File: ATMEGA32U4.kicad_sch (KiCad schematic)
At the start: 4 parts, among them U2 ATMEGA32U4-AU, U3 MIC5219-3_3YM5-TR

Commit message: improvements
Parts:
- added C14, C15, C18: 0.1uF, Capacitor_SMD:C_0805_2012Metric, symbol Device:C_Small
- added C16, C17: 22pF, Capacitor_SMD:C_0805_2012Metric, symbol Device:C_Small
- added C19: 10uF, Capacitor_SMD:C_0805_2012Metric, symbol Device:C_Small
- added C20: 1uF, Capacitor_SMD:C_0805_2012Metric, symbol Device:C_Small
- added J5: Conn_01x04, random-keyboard-parts:JST-SR-4, symbol Connector_Generic:Conn_01x04
- added RC1, RC2: 22, Resistor_SMD:R_0805_2012Metric, symbol Device:R_Small
- added RC3, RC4: 10k, Resistor_SMD:R_0805_2012Metric, symbol Device:R_Small
- added SW1: SW_Push, Button_Switch_SMD:SW_SPST_PTS645, symbol Switch:SW_Push
- added Y1: 16MHz, Crystal:Crystal_SMD_HC49-SD, symbol Device:Crystal
- U2: footprint digikey-footprints:TQFP-44_10x10mm -> Package_DFN_QFN:QFN-44-1EP_7x7mm_P0.5mm_EP5.2x5.2mm; symbol dk_Embedded-Microcontrollers:ATMEGA32U4-AU -> MCU_Microchip_ATmega:ATmega32U4-M
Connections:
- net COL10: now reaches U2.1 (PE6)
- net COL1: now reaches U2.10 (PB2)
- net COL0: now reaches U2.11 (PB3)
- net ROW0: now reaches U2.12 (PB7)
- net at U2.13 (~{RESET}): now also RC3.2, SW1.2
- net +5V: now reaches U2.14 (VCC)
- net +5V: now also U2.2 (UVCC), U2.24 (AVCC), U2.34 (VCC), U2.44 (AVCC), U2.7 (VBUS), C14.1, C15.1, C18.1, C19.1, J5.1 (Pin_1), RC3.1
- net GND: now reaches U2.15 (GND)
- net GND: now also U2.23 (GND), U2.35 (GND), U2.43 (GND), U2.45 (GND), U2.5 (UGND), C14.2, C15.2, C16.2, C17.2, C18.2, C19.2, C20.2, J5.4 (Pin_4), RC4.1, SW1.1
- net at U2.16 (XTAL2): now also C17.1, Y1.2
- net at U2.17 (XTAL1): now also C16.1, Y1.1
- net COL9: now reaches U2.18 (PD0)
- net COL8: now reaches U2.19 (PD1)
- net COL7: now reaches U2.20 (PD2)
- net COL6: now reaches U2.21 (PD3)
- net COL5: now reaches U2.22 (PD5)
- net COL19: now reaches U2.25 (PD4)
- net COL18: now reaches U2.26 (PD6)
- net COL17: now reaches U2.27 (PD7)
- net COL16: now reaches U2.28 (PB4)
- net COL15: now reaches U2.29 (PB5)
- net at U2.3 (D-): now also RC1.1
- net COL14: now reaches U2.30 (PB6)
- net COL13: now reaches U2.31 (PC6)
- net COL12: now reaches U2.32 (PC7)
- net at U2.33 (~{HWB}/PE2): now also RC4.2
- net COL4: now reaches U2.36 (PF7)
- net ROW2: now reaches U2.37 (PF6)
- net ROW3: now reaches U2.38 (PF5)
- net ROW4: now reaches U2.39 (PF4)
- net at U2.4 (D+): now also RC2.1
- net ROW1: now reaches U2.40 (PF1)
- net COL11: now reaches U2.41 (PF0)
- net at U2.6 (UCAP): now also C20.1
- net COL3: now reaches U2.8 (PB0)
- net COL2: now reaches U2.9 (PB1)
- new net D+: J5.3 (Pin_3), RC2.2
- new net D-: J5.2 (Pin_2), RC1.2
- no-connect marks 0 -> 1
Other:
- moved on the sheet: C1, C2, U3

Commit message: improvements
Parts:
- removed C1: 0.1uf, Audio_Module:c_0805, symbol Device:C_Small
- removed C2: 10uf, Audio_Module:c_tant_C, symbol Device:C_Small
- removed U3: MIC5219-3_3YM5-TR, digikey-footprints:SOT-753, symbol dk_PMIC-Voltage-Regulators-Linear:MIC5219-3_3YM5-TR
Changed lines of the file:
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@@
-    )
-  )
-  (symbol (lib_id "Device:C_Small") (at 114.3 26.67 0) (unit 1)
-    (in_bom yes) (on_board yes) (dnp no) (fields_autoplaced)
-    (property "Reference" "C2" (at 116.84 25.4062 0)
-      (effects (font (size 1.27 1.27)) (justify left))
-    )
-    (property "Value" "10uf" (at 116.84 27.9462 0)
-      (effects (font (size 1.27 1.27)) (justify left))
-    )
-    (property "Footprint" "Audio_Module:c_tant_C" (at 114.3 26.67 0)
-      (effects (font (size 1.27 1.27)) hide)
-    )
-    (property "Datasheet" "~" (at 114.3 26.67 0)
-      (effects (font (size 1.27 1.27)) hide)
-    )
-    (property "notes" "ceramic or metal film" (at 114.3 26.67 0)
-      (effects (font (size 1.524 1.524)) hide)
-    )
-    (pin "1")
-    (pin "2")
-    (instances
-      (project "PGA2320"
-        (path "/3c367401-208f-4628-9cce-4b3b1ae65d20"
-          (reference "C2") (unit 1)
-        )
-        (path "/3c367401-208f-4628-9cce-4b3b1ae65d20/da47919b-7b3c-40e2-9d9c-5e15e3d50087"
-          (reference "C13") (unit 1)
-        )
-      )
-      (project "pga2311"
-        (path "/5b7801f4-55a7-4c74-b3bf-bacecbb4cf6a"
-          (reference "C2") (unit 1)
-        )
-      )
     )
   )
@@
         (path "/bdd6f26e-a579-4b76-9cd4-7af86ec9f4f6"
           (reference "#PWR0106") (unit 1)
-        )
-      )
-    )
-  )
-  (symbol (lib_id "Device:C_Small") (at 101.6 26.67 0) (unit 1)
-    (in_bom yes) (on_board yes) (dnp no) (fields_autoplaced)
-    (property "Reference" "C1" (at 104.14 25.4062 0)
-      (effects (font (size 1.27 1.27)) (justify left))
-    )
-    (property "Value" "0.1uf" (at 104.14 27.9462 0)
-      (effects (font (size 1.27 1.27)) (justify left))
-    )
-    (property "Footprint" "Audio_Module:c_0805" (at 101.6 26.67 0)
-      (effects (font (size 1.27 1.27)) hide)
-    )
-    (property "Datasheet" "~" (at 101.6 26.67 0)
-      (effects (font (size 1.27 1.27)) hide)
-    )
-    (property "notes" "tantalum or aluminum electrolytic)" (at 101.6 26.67 0)
-      (effects (font (size 1.524 1.524)) hide)
-    )
-    (pin "1")
-    (pin "2")
-    (instances
-      (project "PGA2320"
-        (path "/3c367401-208f-4628-9cce-4b3b1ae65d20"
-          (reference "C1") (unit 1)
-        )
-        (path "/3c367401-208f-4628-9cce-4b3b1ae65d20/da47919b-7b3c-40e2-9d9c-5e15e3d50087"
-          (reference "C12") (unit 1)
-        )
-      )
-      (project "pga2311"
-        (path "/5b7801f4-55a7-4c74-b3bf-bacecbb4cf6a"
-          (reference "C1") (unit 1)
         )
       )
@@
         )
       )
-    )
-  )
-  (symbol (lib_id "dk_PMIC-Voltage-Regulators-Linear:MIC5219-3_3YM5-TR") (at 85.09 25.4 0) (unit 1)
-    (in_bom yes) (on_board yes) (dnp no) (fields_autoplaced)
-    (property "Reference" "U3" (at 85.09 17.78 0)
-      (effects (font (size 1.524 1.524)))
-    )
-    (property "Value" "MIC5219-3_3YM5-TR" (at 85.09 20.32 0)
-      (effects (font (size 1.524 1.524)))
-    )
-    (property "Footprint" "digikey-footprints:SOT-753" (at 90.17 20.32 0)
-      (effects (font (size 1.524 1.524)) (justify left) hide)
-    )
-    (property "Datasheet" "http://www.microchip.com/mymicrochip/filehandler.aspx?ddocname=en579712" (at 90.17 17.78 0)
-      (effects (font (size 1.524 1.524)) (justify left) hide)
-    )
-    (property "Digi-Key_PN" "576-1281-1-ND" (at 90.17 15.24 0)
-      (effects (font (size 1.524 1.524)) (justify left) hide)
-    )
-    (property "MPN" "MIC5219-3.3YM5-TR" (at 90.17 12.7 0)
-      (effects (font (size 1.524 1.524)) (justify left) hide)
-    )
-    (property "Category" "Integrated Circuits (ICs)" (at 90.17 10.16 0)
-      (effects (font (size 1.524 1.524)) (justify left) hide)
-    )
-    (property "Family" "PMIC - Voltage Regulators - Linear" (at 90.17 7.62 0)
-      (effects (font (size 1.524 1.524)) (justify left) hide)
-    )
-    (property "DK_Datasheet_Link" "http://www.microchip.com/mymicrochip/filehandler.aspx?ddocname=en579712" (at 90.17 5.08 0)
-      (effects (font (size 1.524 1.524)) (justify left) hide)
-    )
-    (property "DK_Detail_Page" "/product-detail/en/microchip-technology/MIC5219-3.3YM5-TR/576-1281-1-ND/771902" (at 90.17 2.54 0)
-      (effects (font (size 1.524 1.524)) (justify left) hide)
-    )
-    (property "Description" "IC REG LINEAR 3.3V 500MA SOT23-5" (at 90.17 0 0)
-      (effects (font (size 1.524 1.524)) (justify left) hide)
-    )
-    (property "Manufacturer" "Microchip Technology" (at 90.17 -2.54 0)
-      (effects (font (size 1.524 1.524)) (justify left) hide)
-    )
-    (property "Status" "Active" (at 90.17 -5.08 0)
-      (effects (font (size 1.524 1.524)) (justify left) hide)
-    )
-    (pin "5")
-    (pin "1")
-    (pin "4")
-    (pin "3")
-    (pin "2")
-    (instances
-      (project "PGA2320"
-        (path "/3c367401-208f-4628-9cce-4b3b1ae65d20/da47919b-7b3c-40e2-9d9c-5e15e3d50087"
-          (reference "U3") (unit 1)
-        )
-      )

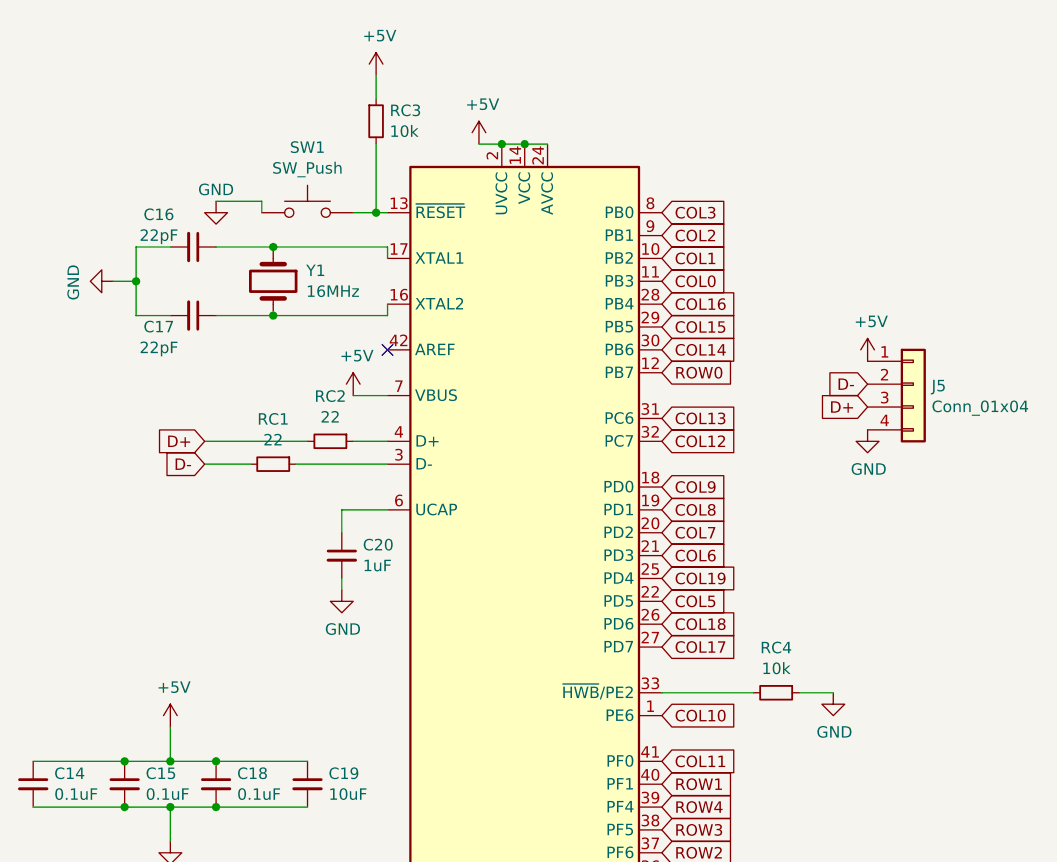
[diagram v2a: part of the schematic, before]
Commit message: add power supply for vdd
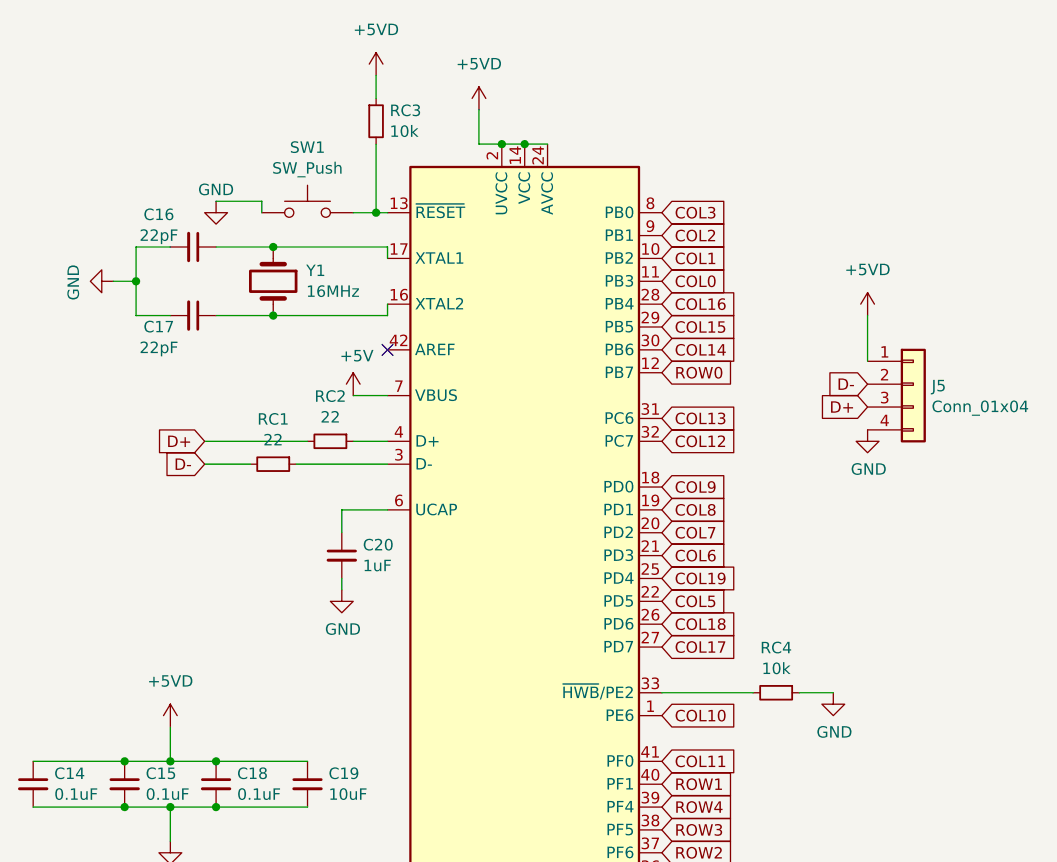
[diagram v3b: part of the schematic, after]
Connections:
- net +5V: no longer C14.1, C15.1, C18.1, C19.1, J5.1 (Pin_1), RC3.1, U2.14 (VCC), U2.2 (UVCC), U2.24 (AVCC), U2.34 (VCC), U2.44 (AVCC)
- new net +5VD: C14.1, C15.1, C18.1, C19.1, J5.1 (Pin_1), RC3.1, U2.14 (VCC), U2.2 (UVCC), U2.24 (AVCC), U2.34 (VCC), U2.44 (AVCC)
